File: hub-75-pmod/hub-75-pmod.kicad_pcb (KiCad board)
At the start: 2 copper layers, 26.7 x 21.6 mm, 13 parts, among them J1 Conn_01x02, J2 Conn_02x08_Odd_Even, J3 PMOD-2x6-FEMALE, J4 Conn_01x02

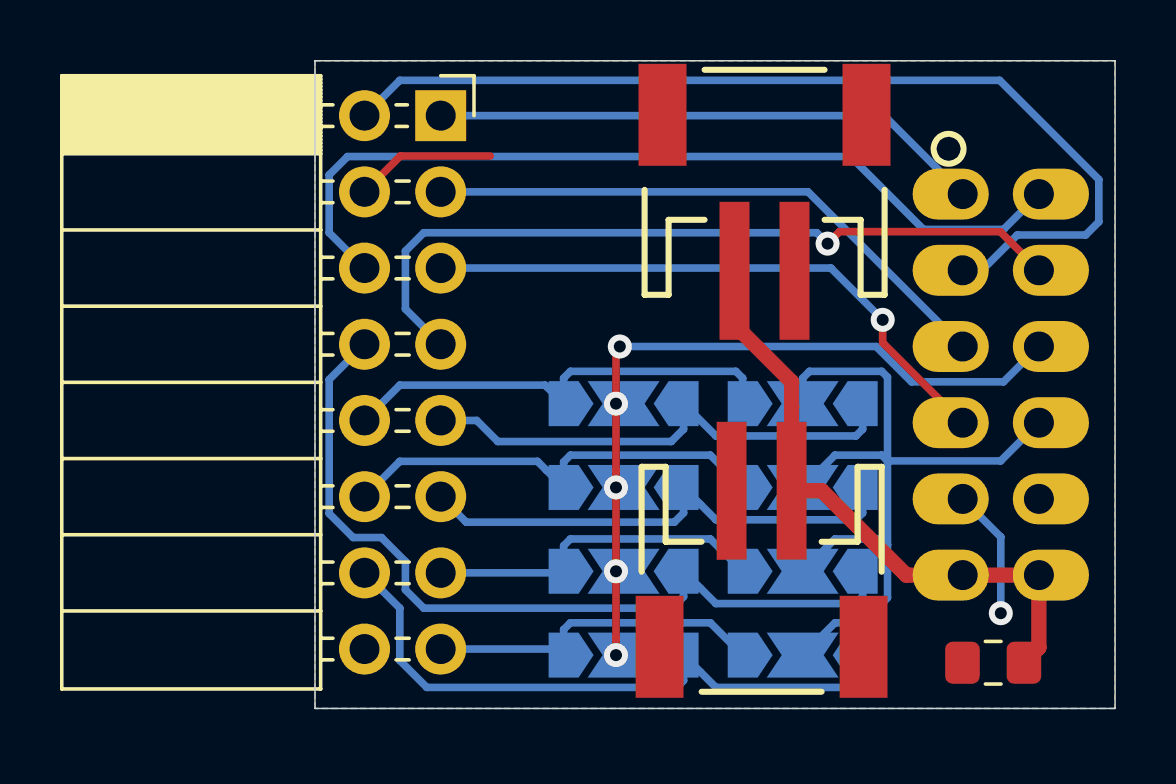
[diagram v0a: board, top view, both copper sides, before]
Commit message: hub75-pmod: fix issues with oval pads for hub75 connector
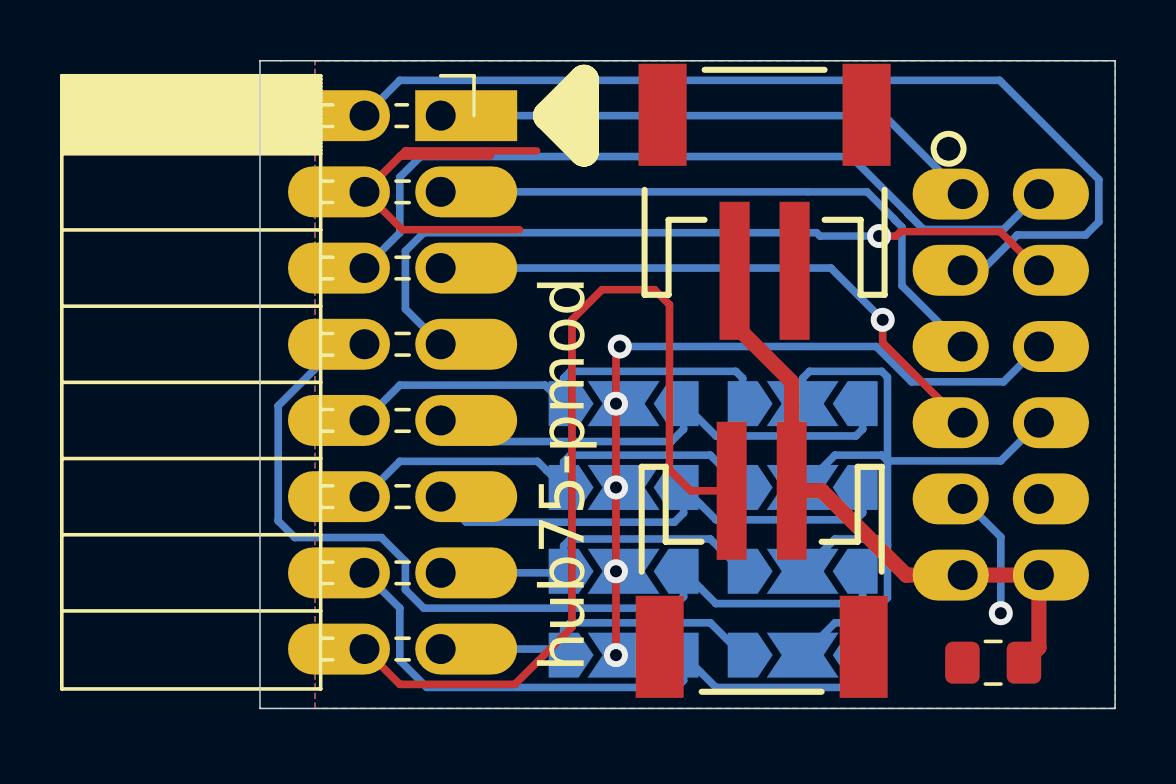
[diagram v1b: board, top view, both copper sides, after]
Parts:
- C1: value C -> 10uF
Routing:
- net GND: track 9.04 -> 51.2 mm
- net E: track 28.2 -> 31.2 mm
- net G1: track 29.0 -> 26.6 mm
- net B0: track 19.5 -> 20.7 mm
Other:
- board size 26.7 x 21.6 mm -> 28.5 x 21.6 mm
- board text added: "apr2020"
- board text removed: "feb2020"
